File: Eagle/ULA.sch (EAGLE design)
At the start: 5 parts, among them IC1 EPM7128, IC2 Soquete ULA

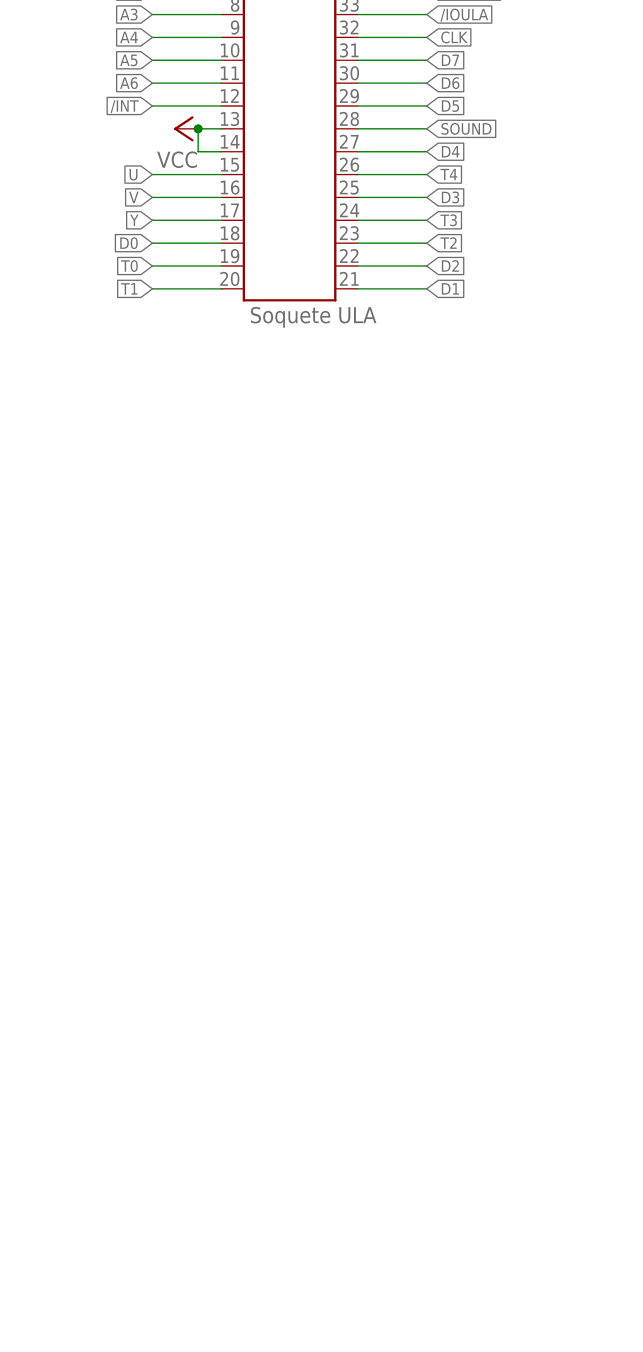
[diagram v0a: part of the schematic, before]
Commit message: added filters for PWM
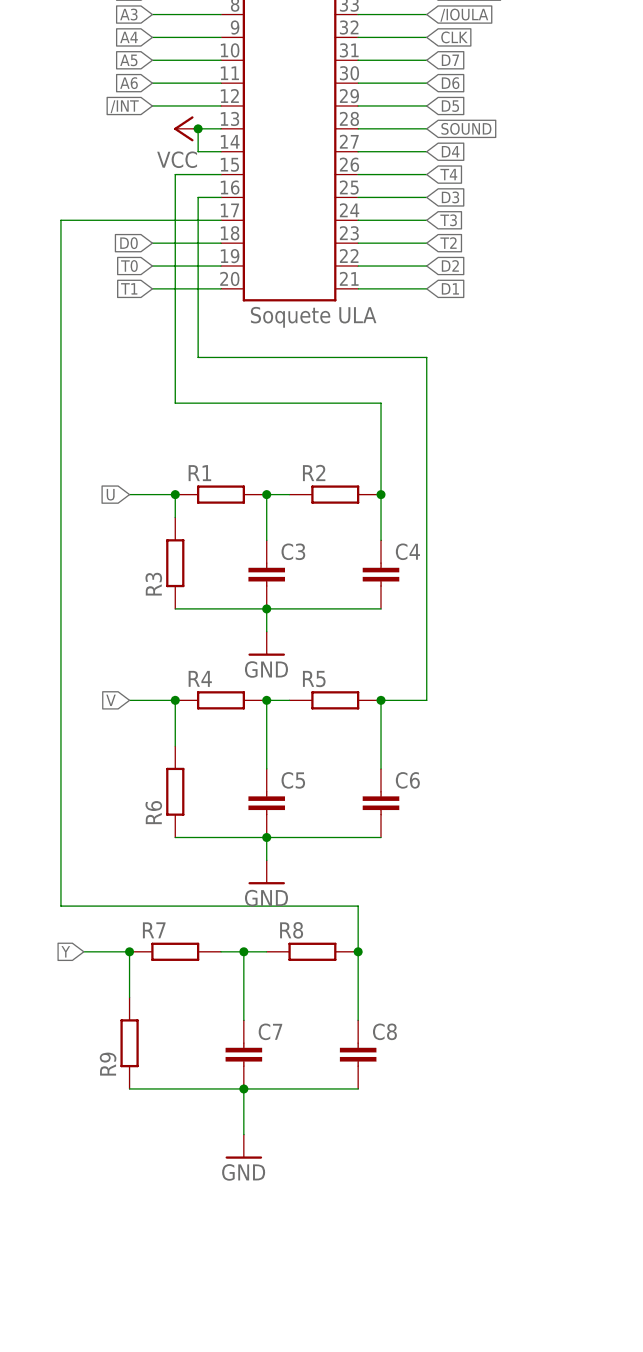
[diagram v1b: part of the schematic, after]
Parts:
- added C3, C4, C5, C6, C7, C8: (no value), rcl:C-EUC0805K
- added R1, R2, R3, R4, R5, R6, R7, R8, R9: (no value), rcl:R-EU_M0805
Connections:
- new net N$1: C5.1, R4.2, R5.1
- new net N$2: C3.1, R1.2, R2.1
- new net N$3: C4.1, IC2.15, R2.2
- new net N$4: C6.1, IC2.16, R5.2
- new net N$5: C7.1, R7.2, R8.1
- new net N$6: C8.1, IC2.17, R8.2
- net GND: now also C3.2, C4.2, C5.2, C6.2, C7.2, C8.2, R3.1, R6.1, R9.1
- net U: now also R1.1, R3.2; no longer IC2.15
- net V: now also R4.1, R6.2; no longer IC2.16
- net Y: now also R7.1, R9.2; no longer IC2.17

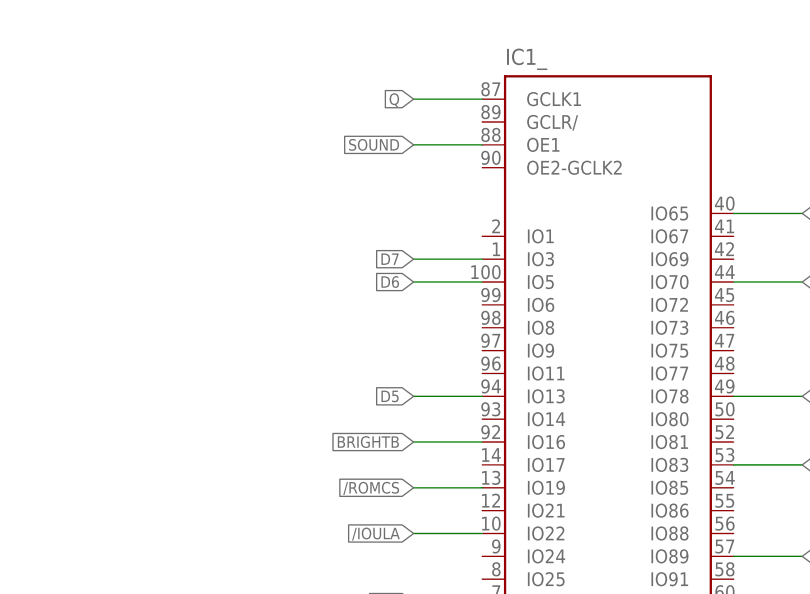
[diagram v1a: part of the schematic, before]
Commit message: CPLD pinout update
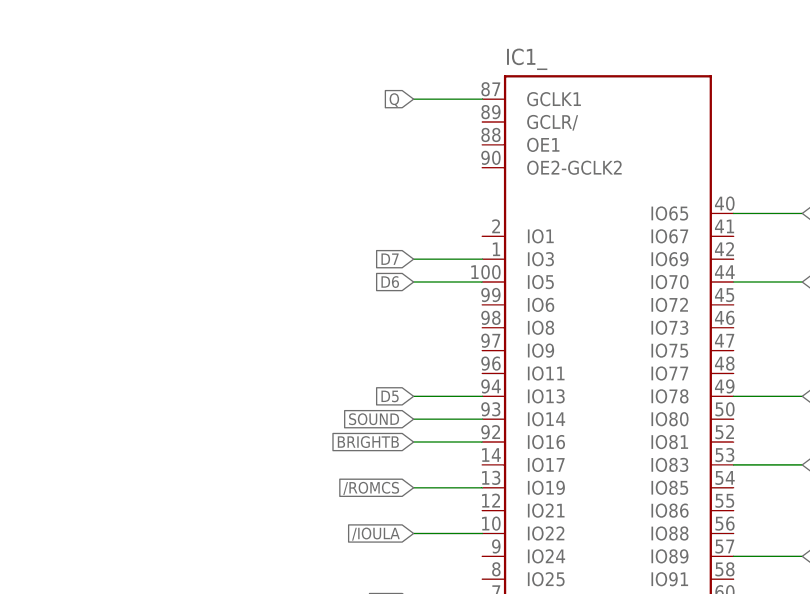
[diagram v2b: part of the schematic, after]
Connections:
- net SOUND: now also IC1_.IO14; no longer IC1_.OE1
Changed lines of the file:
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@@
 </segment>
 <segment>
-<wire x1="144.78" y1="165.1" x2="137.16" y2="165.1" width="0.1524" layer="91"/>
-<label x="137.16" y="165.1" size="1.27" layer="95" rot="R180" xref="yes"/>
-<pinref part="IC1" gate="_" pin="OE1"/>
+<label x="137.16" y="134.62" size="1.27" layer="95" rot="R180" xref="yes"/>
+<wire x1="137.16" y1="134.62" x2="144.78" y2="134.62" width="0.1524" layer="91"/>
+<pinref part="IC1" gate="_" pin="IO14"/>
 </segment>
 </net>
